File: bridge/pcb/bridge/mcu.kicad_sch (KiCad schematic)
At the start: 28 parts, among them J5 Conn_01x04, J6 Conn_01x02, J7 Conn_01x03, J8 Conn_01x02, J9 MCU_Test_Point, SW2 SW_SPST, SW3 SW_SPST, SW4 SW_SPST, U1 L293, U4 ATmega328P-P, U5 L7805, U6 MCP4901

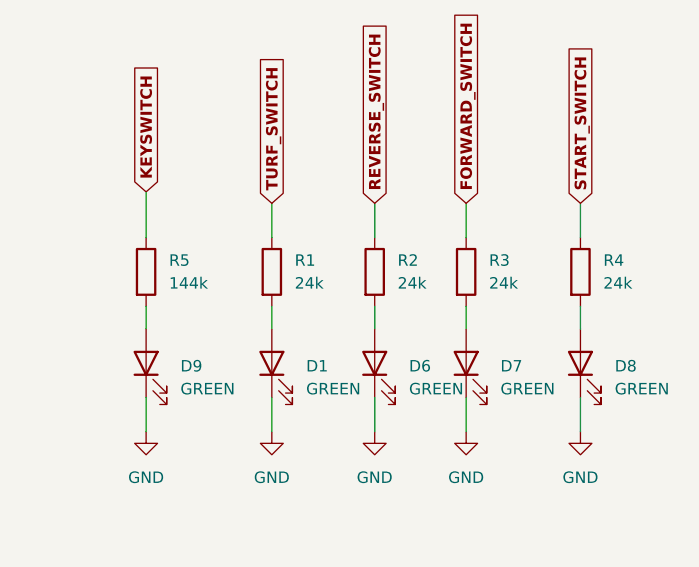
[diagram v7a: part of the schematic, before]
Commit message: Updated resistor values to make LEDs brighter
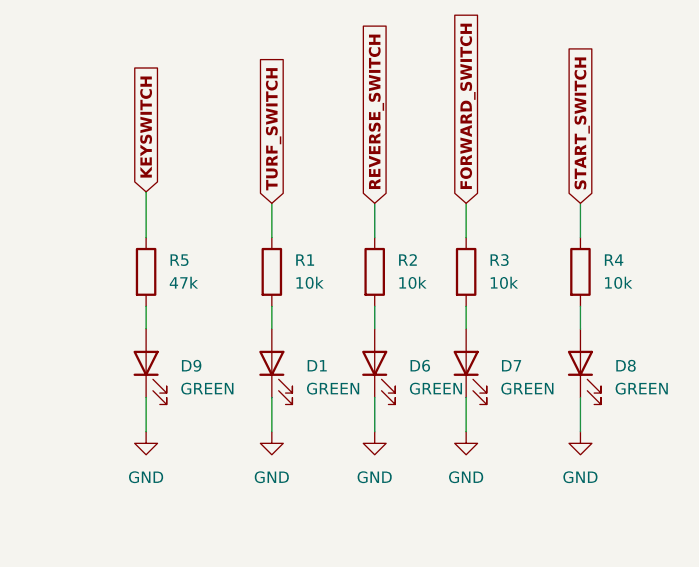
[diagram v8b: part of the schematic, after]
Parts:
- R1, R2, R3, R4: value 24k -> 10k
- R5: value 144k -> 47k
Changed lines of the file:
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@@
       (effects (font (size 1.27 1.27)) (justify left))
     )
-    (property "Value" "24k" (at 257.81 134.62 0)
+    (property "Value" "10k" (at 257.81 134.62 0)
       (effects (font (size 1.27 1.27)) (justify left))
     )
@@
       (effects (font (size 1.27 1.27)) (justify left))
     )
-    (property "Value" "24k" (at 270.51 134.62 0)
+    (property "Value" "10k" (at 270.51 134.62 0)
       (effects (font (size 1.27 1.27)) (justify left))
     )
@@
       (effects (font (size 1.27 1.27)) (justify left))
     )
-    (property "Value" "24k" (at 236.22 134.62 0)
+    (property "Value" "10k" (at 236.22 134.62 0)
       (effects (font (size 1.27 1.27)) (justify left))
     )
@@
       (effects (font (size 1.27 1.27)) (justify left))
     )
-    (property "Value" "144k" (at 222.25 134.62 0)
+    (property "Value" "47k" (at 222.25 134.62 0)
       (effects (font (size 1.27 1.27)) (justify left))
     )
@@
       (effects (font (size 1.27 1.27)) (justify left))
     )
-    (property "Value" "24k" (at 247.65 134.62 0)
-      (effects (font (size 1.27 1.27)) (justify left))
-    )
+    (property "Value" "10k" (at 247.65 134.62 0)
+      (effects (font (size 1.27 1.27)) (justify left))
+    )
